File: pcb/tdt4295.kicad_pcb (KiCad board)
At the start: 6 copper layers, 158 parts, among them J1 DE15_Socket_HighDensity, J2 Conn_02x04_Odd_Even, J3 Conn_ST_STDC14, J4 Micro_SD_Card, J5 USB4110-GF-A, J6 USB4110-GF-A, SW1 SW_BLUE, SW2 SW_BLACK, U1 XC7A50T-FTG256, U2 410-251-B, U3 S70KL1283DPBHV020, U4 W25Q128JVS, U5 TPS54325PWP.d, U6 TPS54294PWP, U7 STM32U595ZJTx, U8 TPS2051CDBV, U9 USBLC6-2SC6, Y1 ASE-20MHz, Y2 16MHz

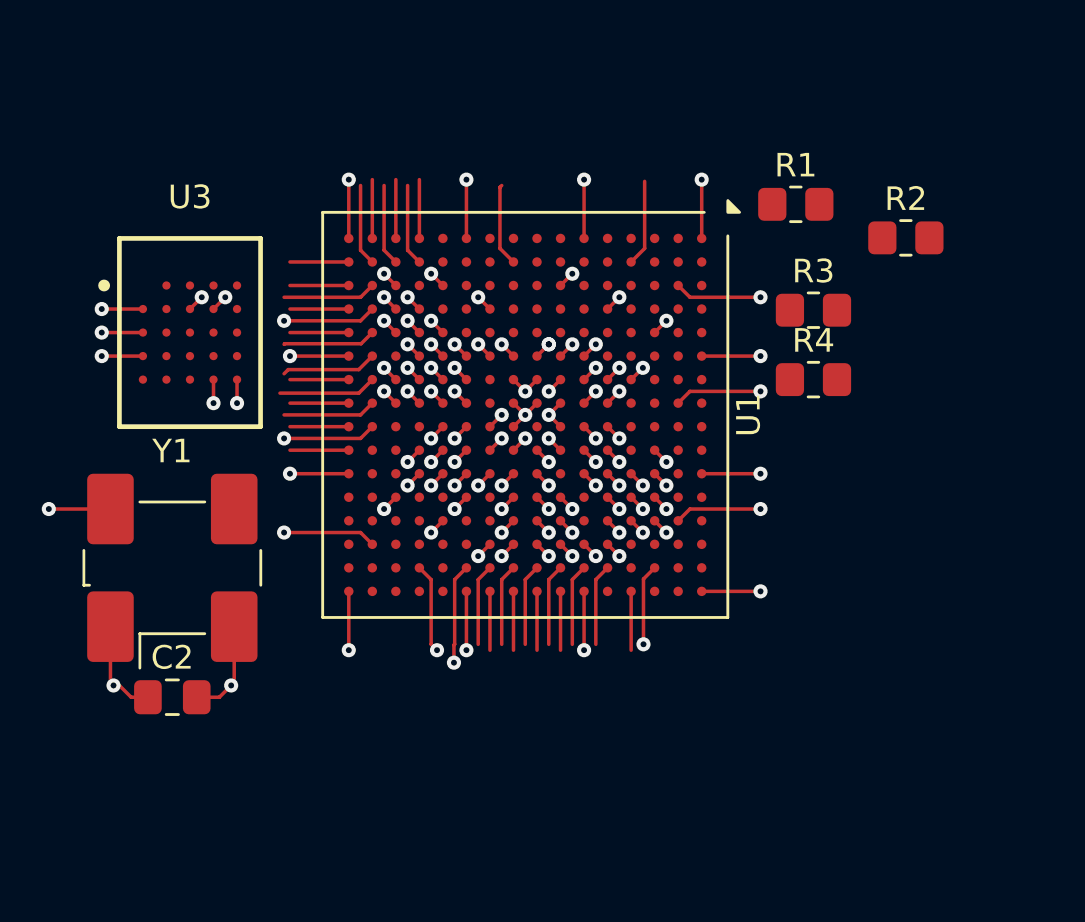
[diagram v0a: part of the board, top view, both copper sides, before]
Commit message: pcb: connect sram+fpga+pullups+clock
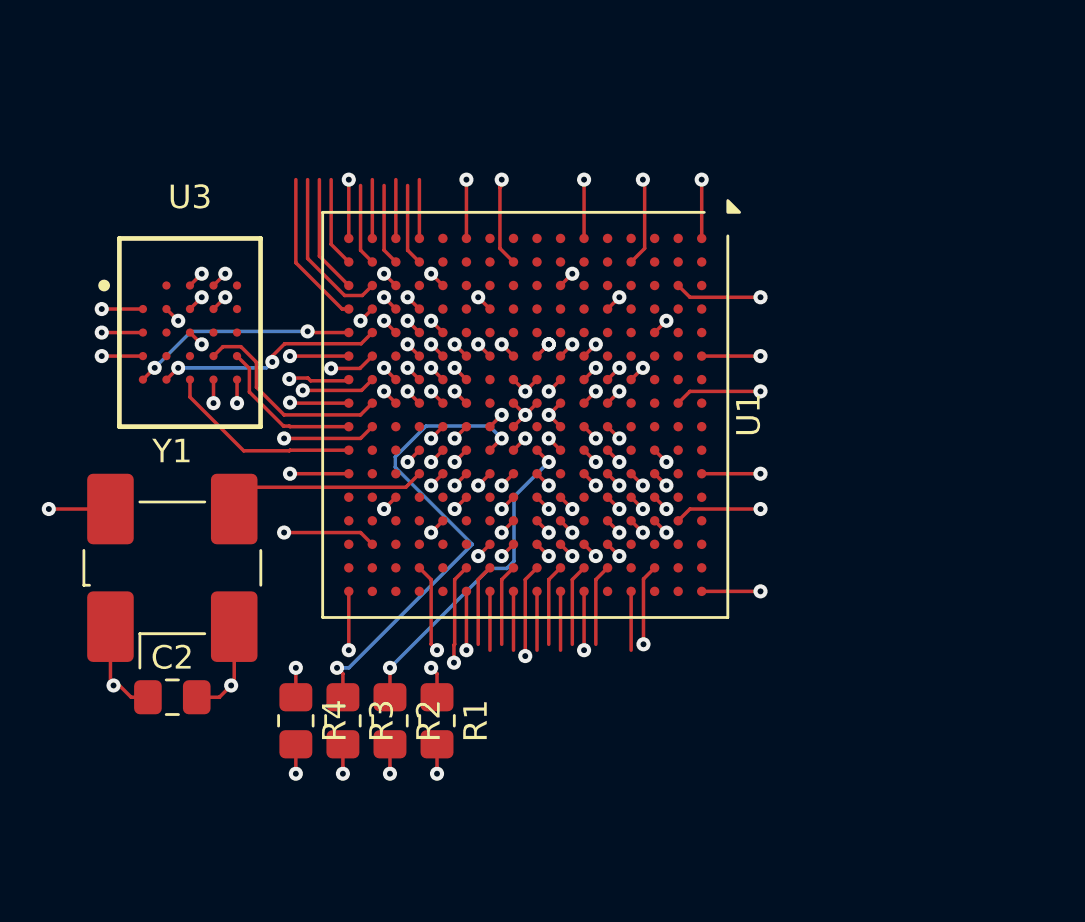
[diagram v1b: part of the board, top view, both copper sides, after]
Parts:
- moved R2 30.0 mm to (110.8, 92.2), turned to -90 degrees
- moved R1 26.7 mm to (112.8, 92.2), turned to -90 degrees
- moved R3 26.5 mm to (108.8, 92.2), turned to -90 degrees
- moved R4 26.3 mm to (106.8, 92.2), turned to -90 degrees
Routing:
- net Net-(U1C-INIT_B_0): track 0.71 -> 20.3 mm, vias 1 -> 2
- net program_b: track 0.71 -> 16.2 mm, vias 1 -> 2
- net done: track 0.71 -> 13.9 mm, vias 1 -> 2
- net Net-(U1C-M0_0): track 0.71 -> 13.5 mm, vias 1 -> 2
- net Net-(U1A-IO_L21N_T3_DQS_A06_D22_14): track 2.50 -> 10.7 mm, vias 0 -> 2
- net Net-(U1A-IO_L13P_T2_MRCC_14): track 0.71 -> 8.49 mm, vias 1 -> 0
- net Net-(U1A-IO_L23N_T3_A02_D18_14): track 2.50 -> 9.62 mm, vias 0 -> 2
- net Net-(U1A-IO_L21P_T3_DQS_14): track 2.50 -> 9.50 mm, vias 0 -> 2
- net Net-(U1A-IO_L24N_T3_A00_D16_14): track 4.16 -> 10.2 mm, vias 0 -> 2
- net Net-(U1A-IO_L22N_T3_A04_D20_14): track 2.50 -> 8.45 mm
- net Net-(U1A-IO_L23P_T3_A03_D19_14): track 3.96 -> 9.72 mm, vias 0 -> 2
- net Net-(U1A-IO_L20N_T3_A07_D23_14): track 3.96 -> 8.96 mm
- net Net-(U1A-IO_L24P_T3_A01_D17_14): track 4.06 -> 8.62 mm, vias 0 -> 2
- net Net-(U1B-IO_L9P_T1_DQS_34): track 2.50 -> 6.60 mm
- net Net-(U1A-IO_L22P_T3_A05_D21_14): track 2.50 -> 6.58 mm
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
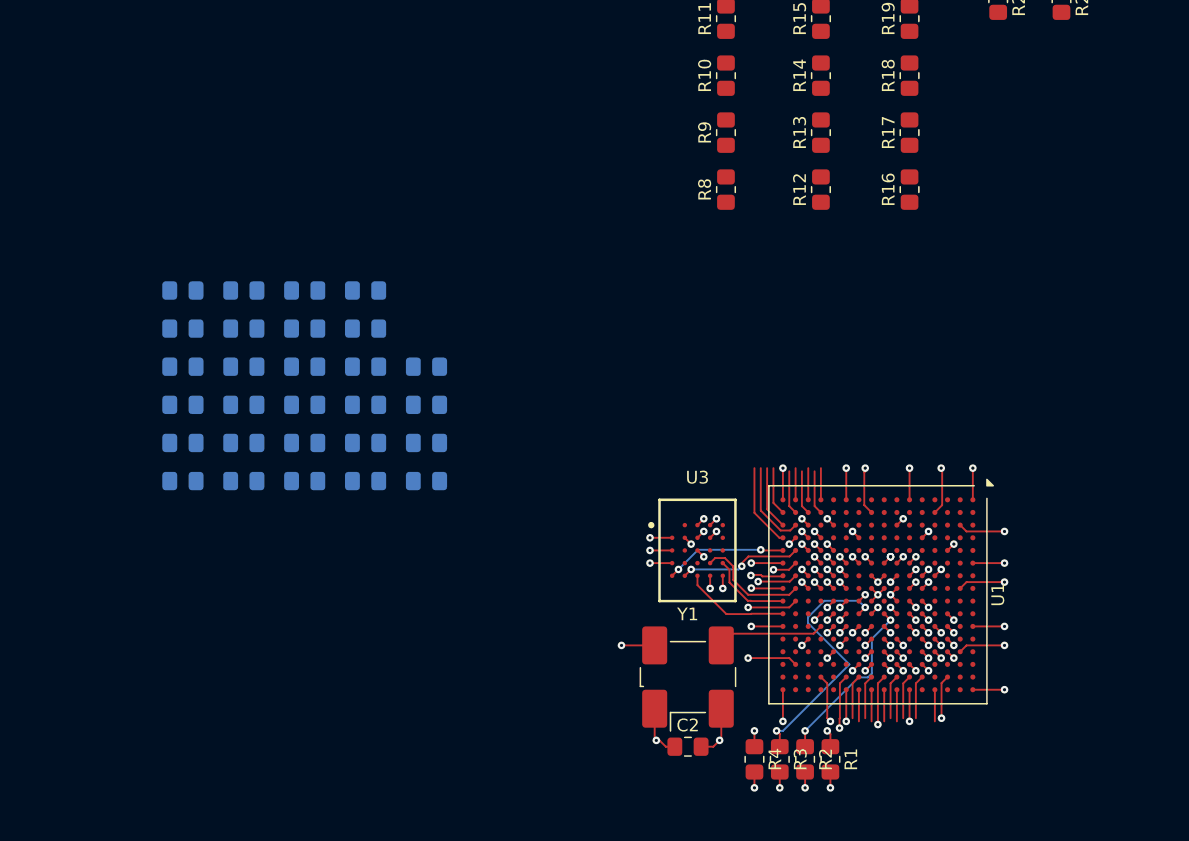
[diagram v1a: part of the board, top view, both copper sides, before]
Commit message: pcb: wip fpga decoupling capacitors
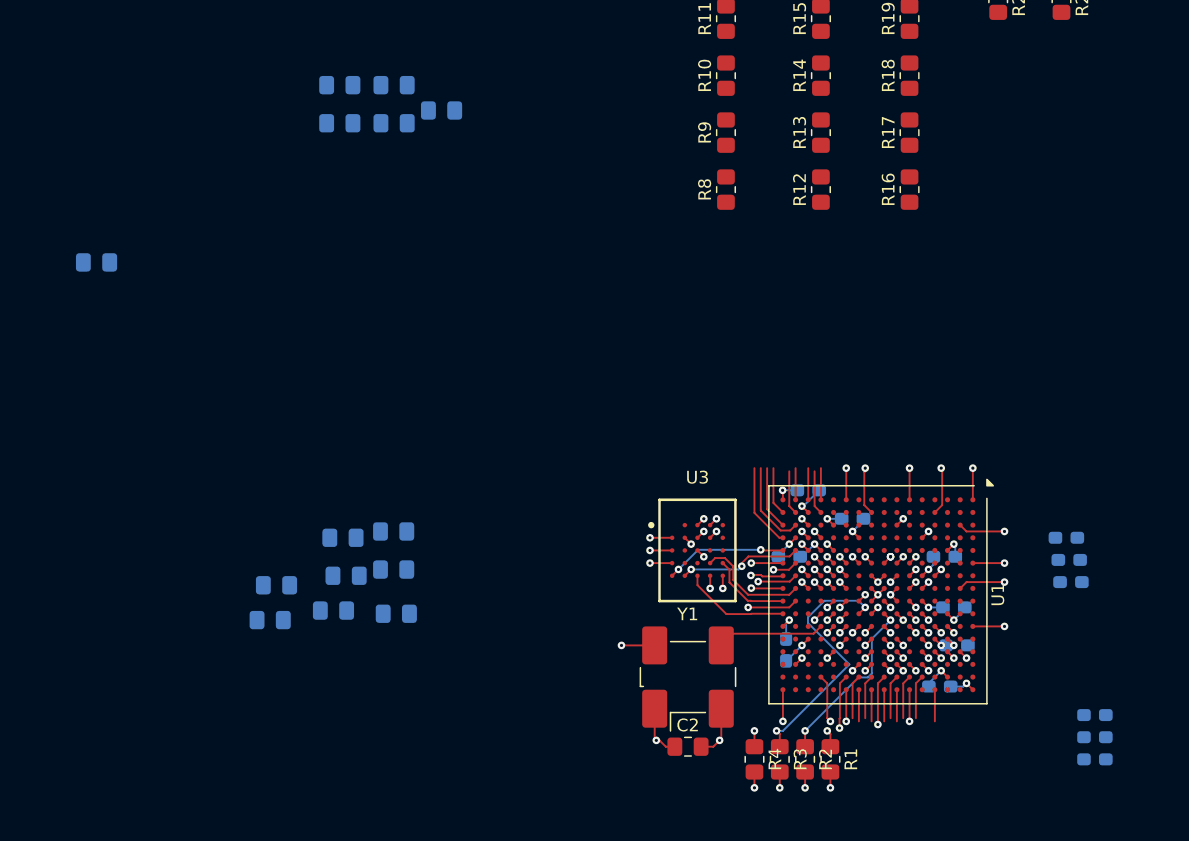
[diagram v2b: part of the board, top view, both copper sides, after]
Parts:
- C10, C14, C16, C17, C20, C23, C26, C27, C28, C29, C30, C7, C8, C9: footprint Capacitor_SMD:C_0805_2012Metric_Pad1.18x1.45mm_HandSolder -> Capacitor_SMD:C_0603_1608Metric_Pad1.08x0.95mm_HandSolder
- moved C26 79.7 mm to (133.6, 92.2)
- moved C28 76.1 mm to (133.6, 88.8)
- moved C30 74.8 mm to (133.6, 90.5)
- moved C27 72.2 mm to (131.8, 78.2)
- moved C29 70.6 mm to (131.6, 76.5)
- moved C14 62.4 mm to (131.4, 74.8)
- moved C23 58.6 mm to (122.8, 83.2)
- moved C17 53.7 mm to (121.4, 86.5)
- moved C9 50.2 mm to (122.5, 80.2)
- moved C8 49.1 mm to (121.8, 76.2), turned to 0 degrees
- moved C20 46.7 mm to (109.5, 76.2), turned to 0 degrees
- moved C16 42.7 mm to (109.2, 83.6), turned to -90 degrees
- moved C7 42.5 mm to (114.5, 73.2), turned to 0 degrees
- moved C10 35.6 mm to (111.0, 71.0), turned to 0 degrees
- moved C18 31.2 mm to (82.0, 41.0)
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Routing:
- net GND: track 277.9 -> 282.9 mm, vias 116 -> 117
- net +3V3: track 43.3 -> 41.2 mm
- net +1V0: track 67.7 -> 68.4 mm, vias 11 -> 12

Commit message: pcb: vga
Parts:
- moved C19 71.4 mm to (125.5, 63.2), turned to -90 degrees
- moved R7 59.9 mm to (140.5, 89.4), turned to 180 degrees
- moved R24 59.1 mm to (129.1, 70.5), turned to -90 degrees
- moved C3 57.9 mm to (111.5, 83.2), turned to 0 degrees
- moved R6 57.8 mm to (135.5, 89.4), turned to 180 degrees
- moved R23 57.0 mm to (126.6, 70.5), turned to -90 degrees
- moved C18 55.4 mm to (118.2, 82.9)
- moved C25 52.1 mm to (120.2, 68.9), turned to -90 degrees
- moved C24 51.9 mm to (120.2, 77.7), turned to -90 degrees
- moved R5 50.2 mm to (145.8, 89.4), turned to 180 degrees
- moved D2 47.5 mm to (91.5, 101.4)
- moved D4 47.5 mm to (75.0, 139.9)
- moved J4 47.5 mm to (74.9, 90.0)
- moved C35 47.5 mm to (95.1, 138.2)
- moved C40 47.5 mm to (111.1, 131.7)
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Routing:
- net Net-(U1C-TDI_0): track 0.71 -> 65.0 mm, vias 1 -> 2
- net Net-(U1C-TDO_0): track 0.71 -> 61.8 mm, vias 1 -> 2
- net /fpga/RED_ANALOG: track 0.00 -> 58.5 mm
- net Net-(U1C-TCK_0): track 0.71 -> 51.8 mm, vias 1 -> 2
- net /fpga/GREEN_ANALOG: track 0.00 -> 48.5 mm
- net Net-(U1C-TMS_0): track 0.71 -> 44.5 mm, vias 1 -> 2
- net /fpga/BLUE_ANALOG: track 0.00 -> 39.7 mm
- net Net-(U1B-IO_L4P_T0_34): track 2.50 -> 38.3 mm, vias 0 -> 2
- net Net-(U1B-IO_L3N_T0_DQS_34): track 3.46 -> 35.8 mm, vias 0 -> 2
- net Net-(U1A-IO_L6P_T0_FCS_B_14): track 0.71 -> 28.6 mm, vias 1 -> 2
- net Net-(U1A-IO_L2P_T0_D02_14): track 3.46 -> 28.7 mm, vias 0 -> 2
- net GND: track 282.9 -> 305.5 mm, vias 117 -> 136
- net +3V3: track 41.2 -> 63.6 mm, vias 25 -> 37
- net Net-(U1A-IO_L2N_T0_D03_14): track 2.50 -> 23.2 mm
- net Net-(U1A-IO_L1P_T0_D00_MOSI_14): track 0.71 -> 21.1 mm, vias 1 -> 2
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
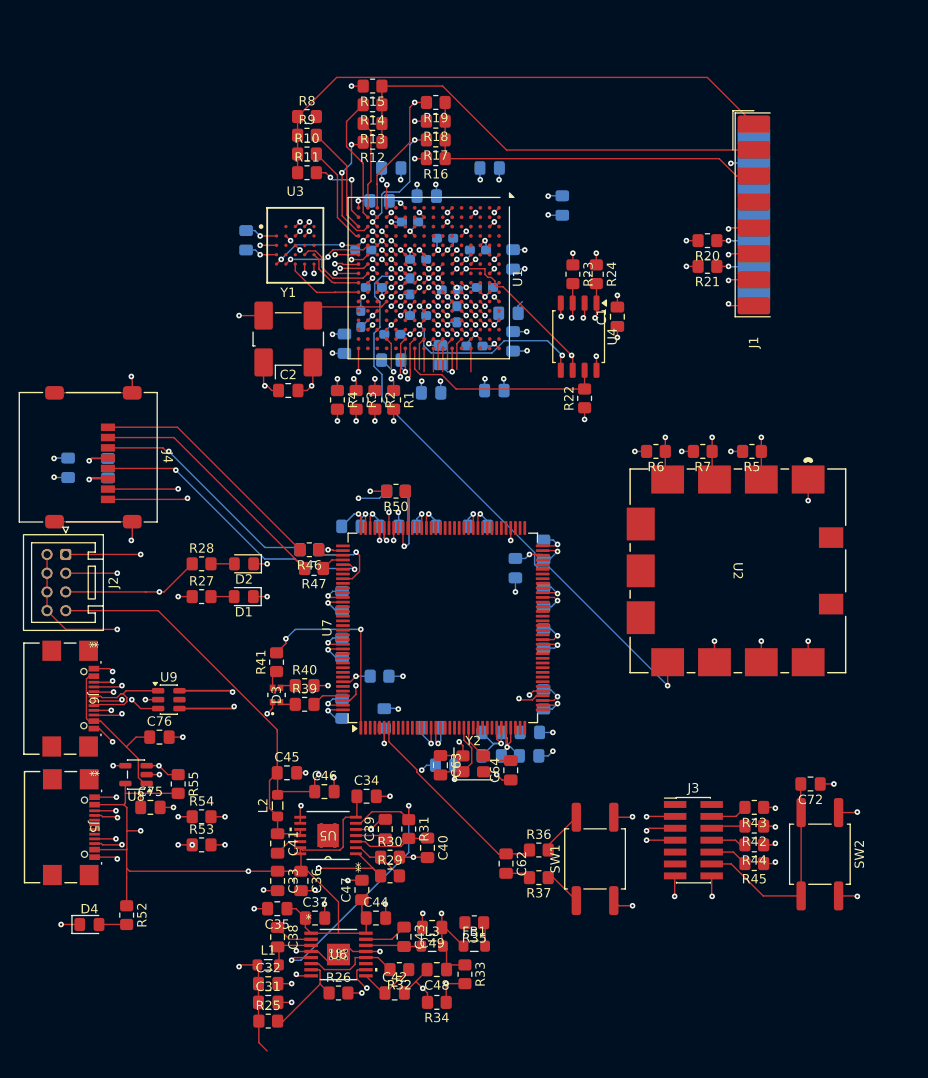
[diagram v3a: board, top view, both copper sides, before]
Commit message: pcb: add board and pwr/gnd planes
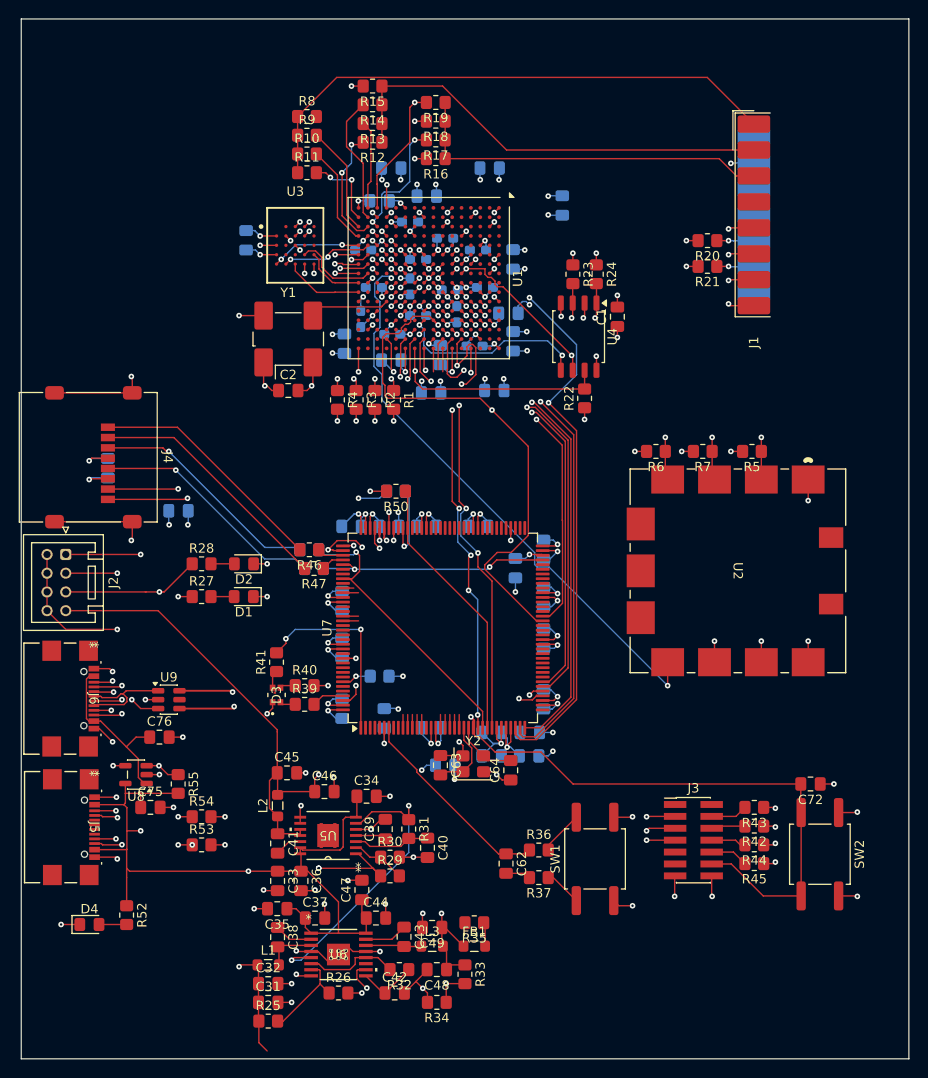
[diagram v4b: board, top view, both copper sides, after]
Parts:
- moved C73 12.6 mm to (84.5, 95.8), turned to 180 degrees
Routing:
- net CC1: track 37.2 -> 106.0 mm, vias 3 -> 4
- net Net-(U7-PA13): track 1.29 -> 69.7 mm, vias 1 -> 2
- net P1_NCS: track 0.71 -> 68.5 mm, vias 1 -> 2
- net P2_NCS: track 0.71 -> 64.5 mm, vias 1 -> 3
- net Net-(U7-PA14): track 1.29 -> 62.6 mm, vias 1 -> 2
- net SPI1_SCK: track 3.46 -> 62.1 mm, vias 0 -> 3
- net P2_IO4: track 0.71 -> 56.6 mm, vias 1 -> 2
- net Net-(U7-PB3): track 1.32 -> 55.7 mm, vias 1 -> 2
- net P2_IO5: track 0.71 -> 52.7 mm, vias 1 -> 2
- net SPI1_MISO: track 3.46 -> 48.5 mm, vias 0 -> 2
- net P1_IO6: track 3.46 -> 45.7 mm, vias 0 -> 4
- net P1_IO7: track 2.50 -> 44.6 mm, vias 0 -> 6
- net Net-(J3-~{RST}): track 22.9 -> 63.3 mm, vias 0 -> 1
- net SPI1_MOSI: track 2.50 -> 42.7 mm, vias 0 -> 2
- net SPI_MISO: track 4.03 -> 28.9 mm
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- added copper zone on In2.Cu, net +3.3V
- added copper zone on In2.Cu, net +3V3
- added copper zone on In1.Cu, net GND
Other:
- board outline added: 94.8 x 111 mm

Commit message: pcb
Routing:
- net +3V3: track 63.6 -> 79.6 mm
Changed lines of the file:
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@@
 		(capping no)
 		(filling no)
+		(zone_defaults)
 		(pcbplotparams
 			(layerselection 0x00000000_00000000_55555555_5755f5ff)
@@
 	)
 	(segment
+		(start 103.5 86)
+		(end 105 87.5)
+		(width 0.15)
+		(layer "F.Cu")
+		(net "+3V3")
+	)
+	(segment
 		(start 107.5 84.9125)
 		(end 107.5 86.1625)
@@
 	)
 	(segment
+		(start 89.9125 79.9125)
+		(end 89.5 79.5)
+		(width 0.15)
+		(layer "F.Cu")
+		(net "+3V3")
+	)
+	(segment
 		(start 108.75 78.4125)
 		(end 108.75 80.9125)
@@
 	)
 	(segment
+		(start 103.5 84.9125)
+		(end 103.5 86)
+		(width 0.15)
+		(layer "F.Cu")
+		(net "+3V3")
+	)
+	(segment
 		(start 93.62 74.9125)
 		(end 91 74.9125)
@@
 	)
 	(segment
+		(start 101.5 84.9125)
+		(end 107.5 84.9125)
+		(width 0.15)
+		(layer "F.Cu")
+		(net "+3V3")
+	)
+	(segment
 		(start 98 66.4125)
 		(end 98.5 65.9125)
@@
 	)
 	(segment
+		(start 101.5 86.1625)
+		(end 102.1625 86.1625)
+		(width 0.15)
+		(layer "F.Cu")
+		(net "+3V3")
+	)
+	(segment
 		(start 105.75 69.4125)
 		(end 105.25 68.9125)
@@
 	)
 	(segment
+		(start 102.1625 86.1625)
+		(end 103.5 87.5)
+		(width 0.15)
+		(layer "F.Cu")
+		(net "+3V3")
+	)
+	(segment
+		(start 93.62 79.9125)
+		(end 89.9125 79.9125)
+		(width 0.15)
+		(layer "F.Cu")
+		(net "+3V3")
+	)
+	(segment
 		(start 127.885 84.75)
 		(end 127.885 86)
@@
 		(width 0.15)
 		(layer "F.Cu")
+		(net "Net-(J6-DN1)")
+	)
+	(segment
+		(start 75.505 115.052499)
+		(end 75.505 115.1751)
+		(width 0.15)
+		(layer "F.Cu")
